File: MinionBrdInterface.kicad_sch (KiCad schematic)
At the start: 26 parts, among them J4 Conn_02x05_Top_Bottom, J6 Conn_01x04, U1 EL3H7, U16 EL3H7, U2 EL3H7, U20 EL3H7, U21 EL3H7, U22 EL3H7, U3 EL3H7, U4 EL3H7

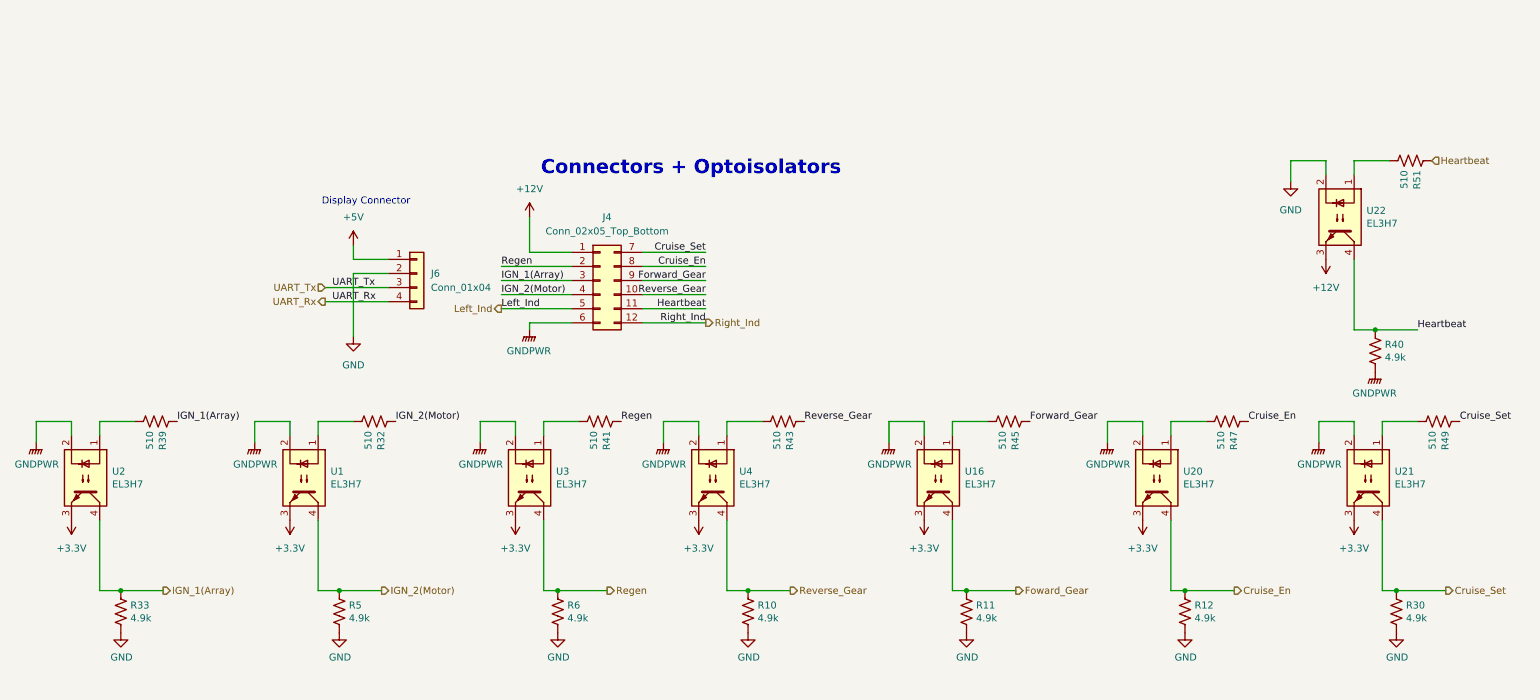
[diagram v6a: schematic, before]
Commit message: Renamed local net labels to be different from hierarchical ones in the MinionBrdInterface so that they aren't connected. Changed Regen input to BPS Hazard light since we aren't using regen but will be alerting the driver of BPS faults.
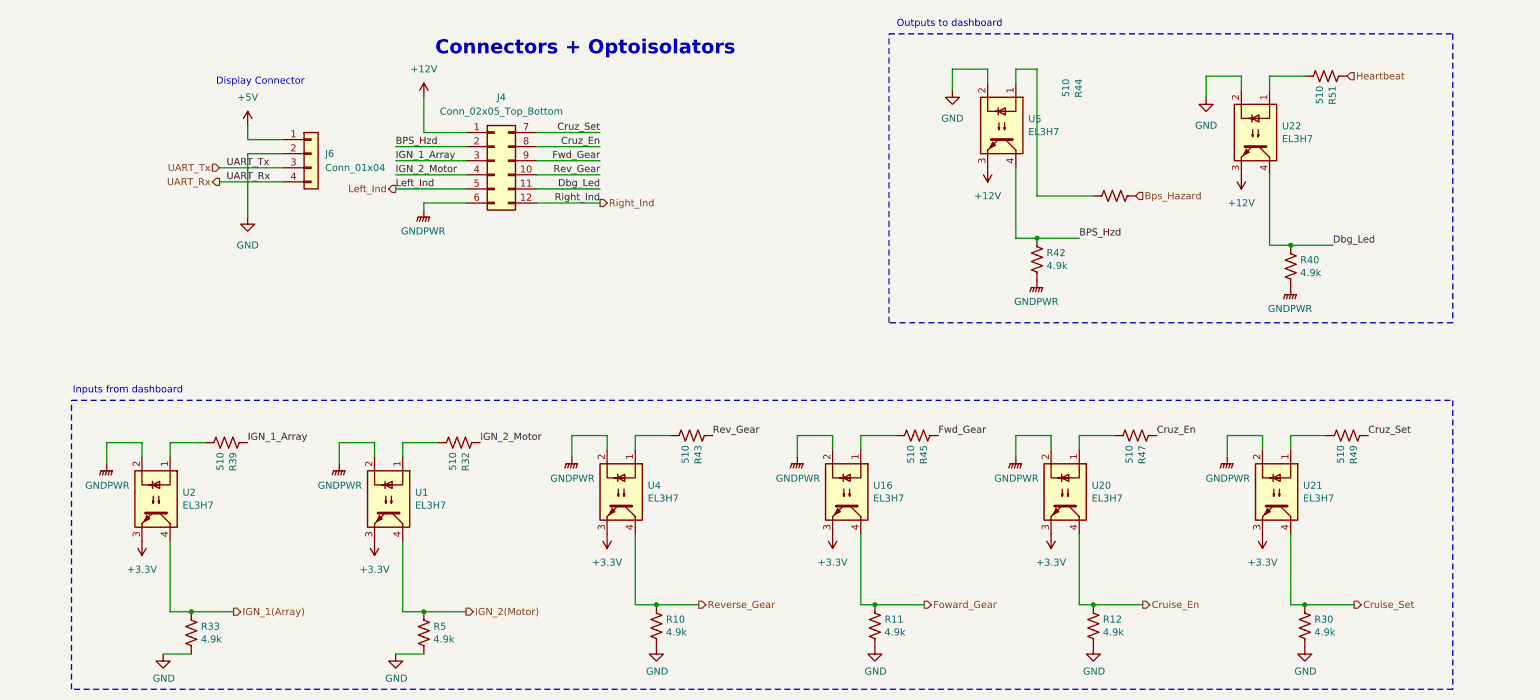
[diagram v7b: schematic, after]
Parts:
- removed R41: 510, Resistor_SMD:R_0805_2012Metric, symbol Device:R_US
- removed R6: 4.9k, Resistor_SMD:R_0805_2012Metric, symbol Device:R_US
- removed U3: EL3H7, Package_SO:SOP-4_4.4x2.6mm_P1.27mm, symbol Isolator:SFH617A-1
- added R42: 4.9k, Resistor_SMD:R_0805_2012Metric, symbol Device:R_US
- added R44: 510, Resistor_SMD:R_0805_2012Metric, symbol Device:R_US
- added U5: EL3H7, Package_SO:SOP-4_4.4x2.6mm_P1.27mm, symbol Isolator:SFH617A-1
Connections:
- net +12V: now also U5.3
- net Cruise_En: no longer J4.8 (Pin_8), R47.1
- net Cruise_Set: no longer J4.7 (Pin_7), R49.1
- net GND: now also U5.2
- net GNDPWR: now also R42.2
- net Heartbeat: no longer J4.11 (Pin_11), R40.1, U22.4
- net IGN_1(Array): no longer J4.3 (Pin_3), R39.1
- net IGN_2(Motor): no longer J4.4 (Pin_4), R32.1
- net Reverse_Gear: no longer J4.10 (Pin_10), R43.1
- net Forward_Gear renamed Fwd_Gear
- net Regen renamed BPS_Hzd
- net BPS_Hzd: now also R42.1, U5.4
- new net: R44.2, U5.1
- new net Bps_Hazard: R44.1
- new net Cruz_En: J4.8 (Pin_8), R47.1
- new net Cruz_Set: J4.7 (Pin_7), R49.1
- new net Dbg_Led: J4.11 (Pin_11), R40.1, U22.4
- new net IGN_1_Array: J4.3 (Pin_3), R39.1
- new net IGN_2_Motor: J4.4 (Pin_4), R32.1
- new net Rev_Gear: J4.10 (Pin_10), R43.1
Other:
- note added: "Inputs from dashboard"
- note added: "Outputs to dashboard"
- moved on the sheet: J4, J6, R10, R11, R12, R30, R32, R33, R39, R40, R43, R45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

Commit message: Flipped optoisolators, changed resistor values, added second connector to motor can and disconnected shield pins for now since I haven't seen them used (will chack against old version to see what the circuit looked like), copied power-in circuit from contactor board, added optoisolator to timer and blinker light connection.
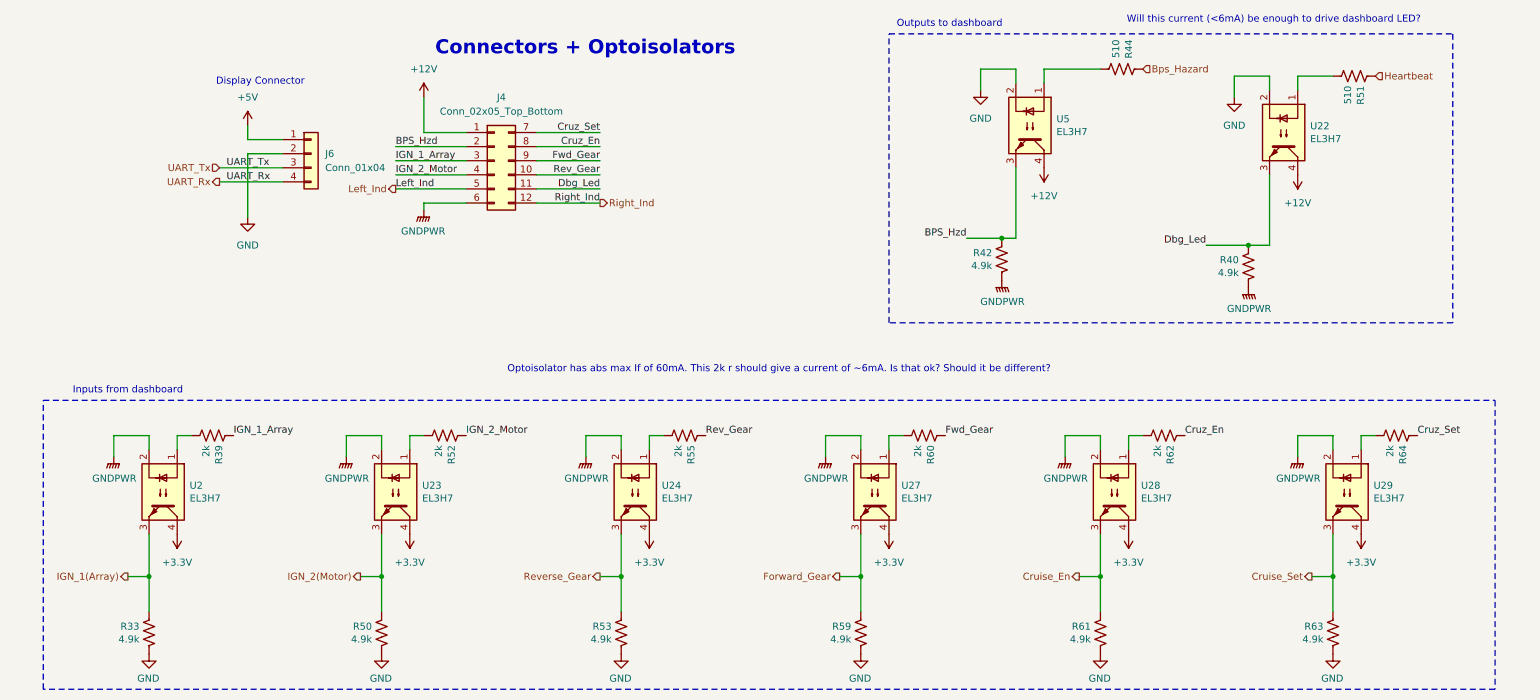
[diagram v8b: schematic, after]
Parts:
- removed R10, R11, R12, R30, R5: 4.9k, Resistor_SMD:R_0805_2012Metric, symbol Device:R_US
- removed R32, R43, R45, R47, R49: 510, Resistor_SMD:R_0805_2012Metric, symbol Device:R_US
- removed U1, U16, U20, U21, U4: EL3H7, Package_SO:SOP-4_4.4x2.6mm_P1.27mm, symbol Isolator:SFH617A-1
- added R50, R53, R59, R61, R63: 4.9k, Resistor_SMD:R_0805_2012Metric, symbol Device:R_US
- added R52, R55, R60, R62, R64: 2k, Resistor_SMD:R_0805_2012Metric, symbol Device:R_US
- added U23, U24, U27, U28, U29: EL3H7, Package_DIP:DIP-4_W7.62mm, symbol Isolator:SFH617A-1
- R39: value 510 -> 2k
- U2, U22, U5: footprint Package_SO:SOP-4_4.4x2.6mm_P1.27mm -> Package_DIP:DIP-4_W7.62mm
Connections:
- net +12V: now also U22.4, U5.4; no longer U22.3, U5.3
- net +3.3V: now also U2.4, U23.4, U24.4, U27.4, U28.4, U29.4; no longer U2.3
- net BPS_Hzd: now also U5.3; no longer U5.4
- net Cruise_En: now also R61.1, U28.3
- net Cruise_Set: now also R63.1, U29.3
- net Cruz_En: now also R62.1
- net Cruz_Set: now also R64.1
- net Dbg_Led: now also U22.3; no longer U22.4
- net Fwd_Gear: now also R60.1
- net GND: now also R50.2, R53.2, R59.2, R61.2, R63.2
- net GNDPWR: now also U23.2, U24.2, U27.2, U28.2, U29.2
- net IGN_1(Array): now also U2.3; no longer U2.4
- net IGN_2(Motor): now also R50.1, U23.3
- net IGN_2_Motor: now also R52.1
- net Rev_Gear: now also R55.1
- net Reverse_Gear: now also R53.1, U24.3
- new net: R60.2, U27.1
- new net: R55.2, U24.1
- new net: R64.2, U29.1
- new net: R52.2, U23.1
- new net: R62.2, U28.1
- new net Forward_Gear: R59.1, U27.3
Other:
- note added: "Optoisolator has abs max If of 60mA. This 2k r should give a current of ~6mA. Is that ok? Should it be different?"
- note added: "Will this current (<6mA) be enough to drive dashboard LED?"
- moved on the sheet: R33, R39, R40, R42, R44, R51, U2, U22, U5
